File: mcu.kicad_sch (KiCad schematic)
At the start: 63 parts, among them J1 Conn_01x04_Pin, J2 USB_C_Receptacle_USB2.0_16P, J3 AudioJack2_Ground_Switch, J4 Conn_01x04_Pin, J5 Conn_01x04_Pin, J6 AudioJack2_Ground_Switch, J7 AudioJack2_Ground_Switch, Q1 BSS138, SW2 BTN, SW3 BTN, SW4 RotaryEncoder_Switch, SW5 BTN, U3 LM358B, U4 STM32G0B1RBTx

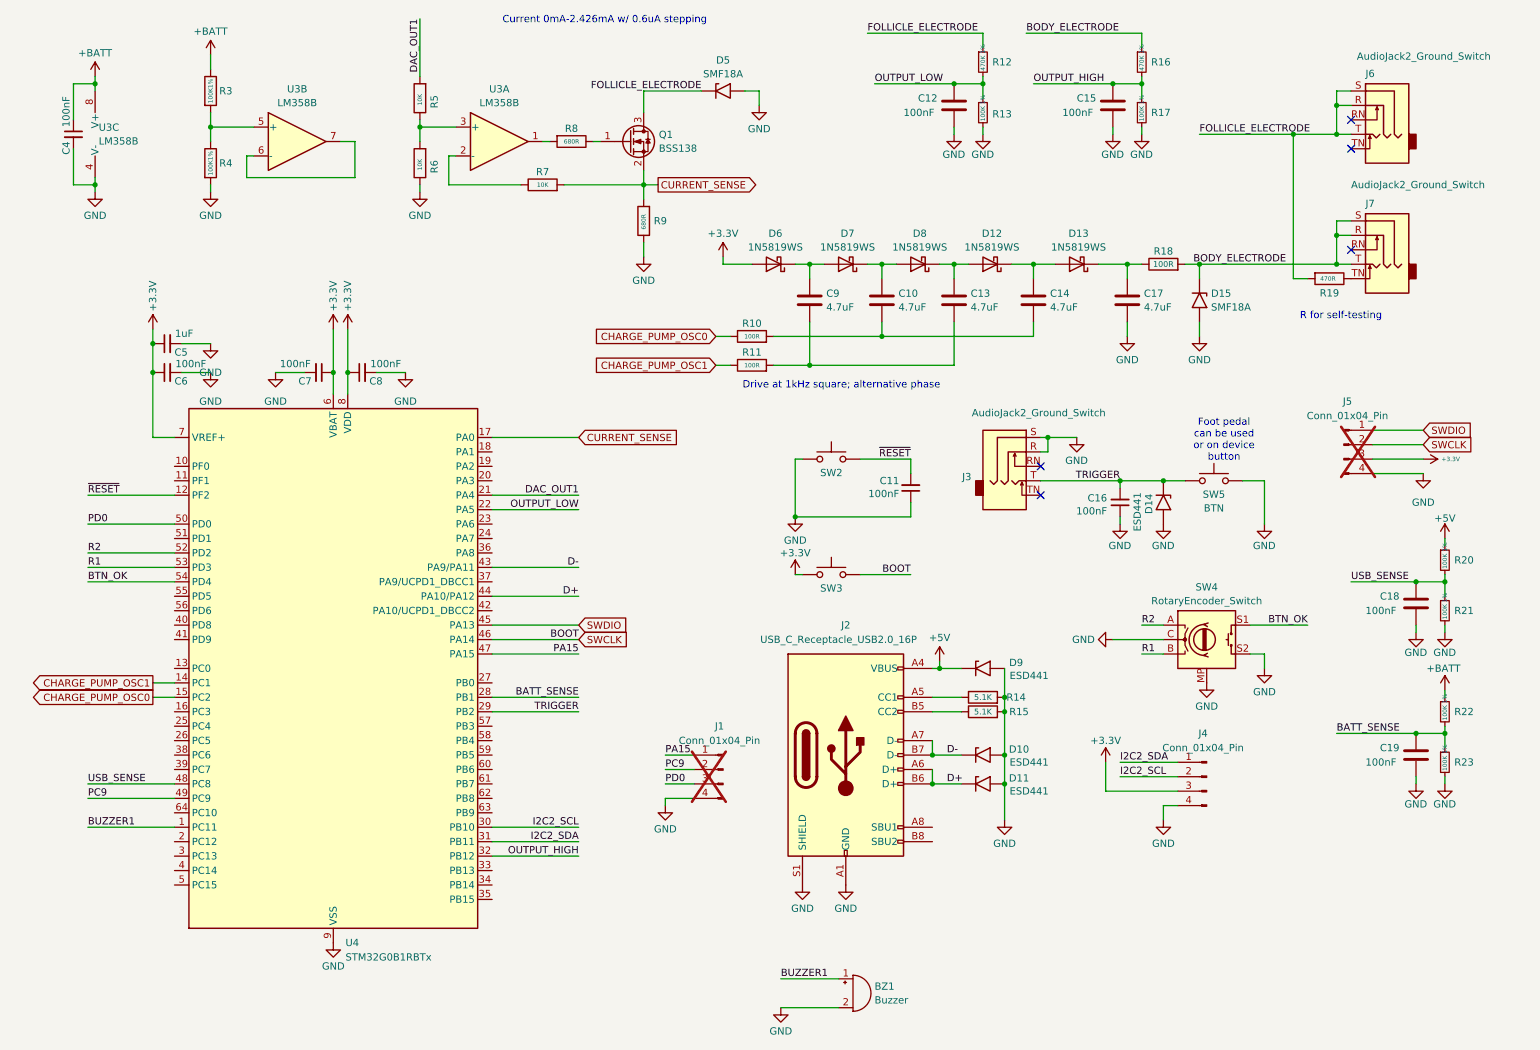
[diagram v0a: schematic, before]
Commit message: Updated buzzer and jack detection
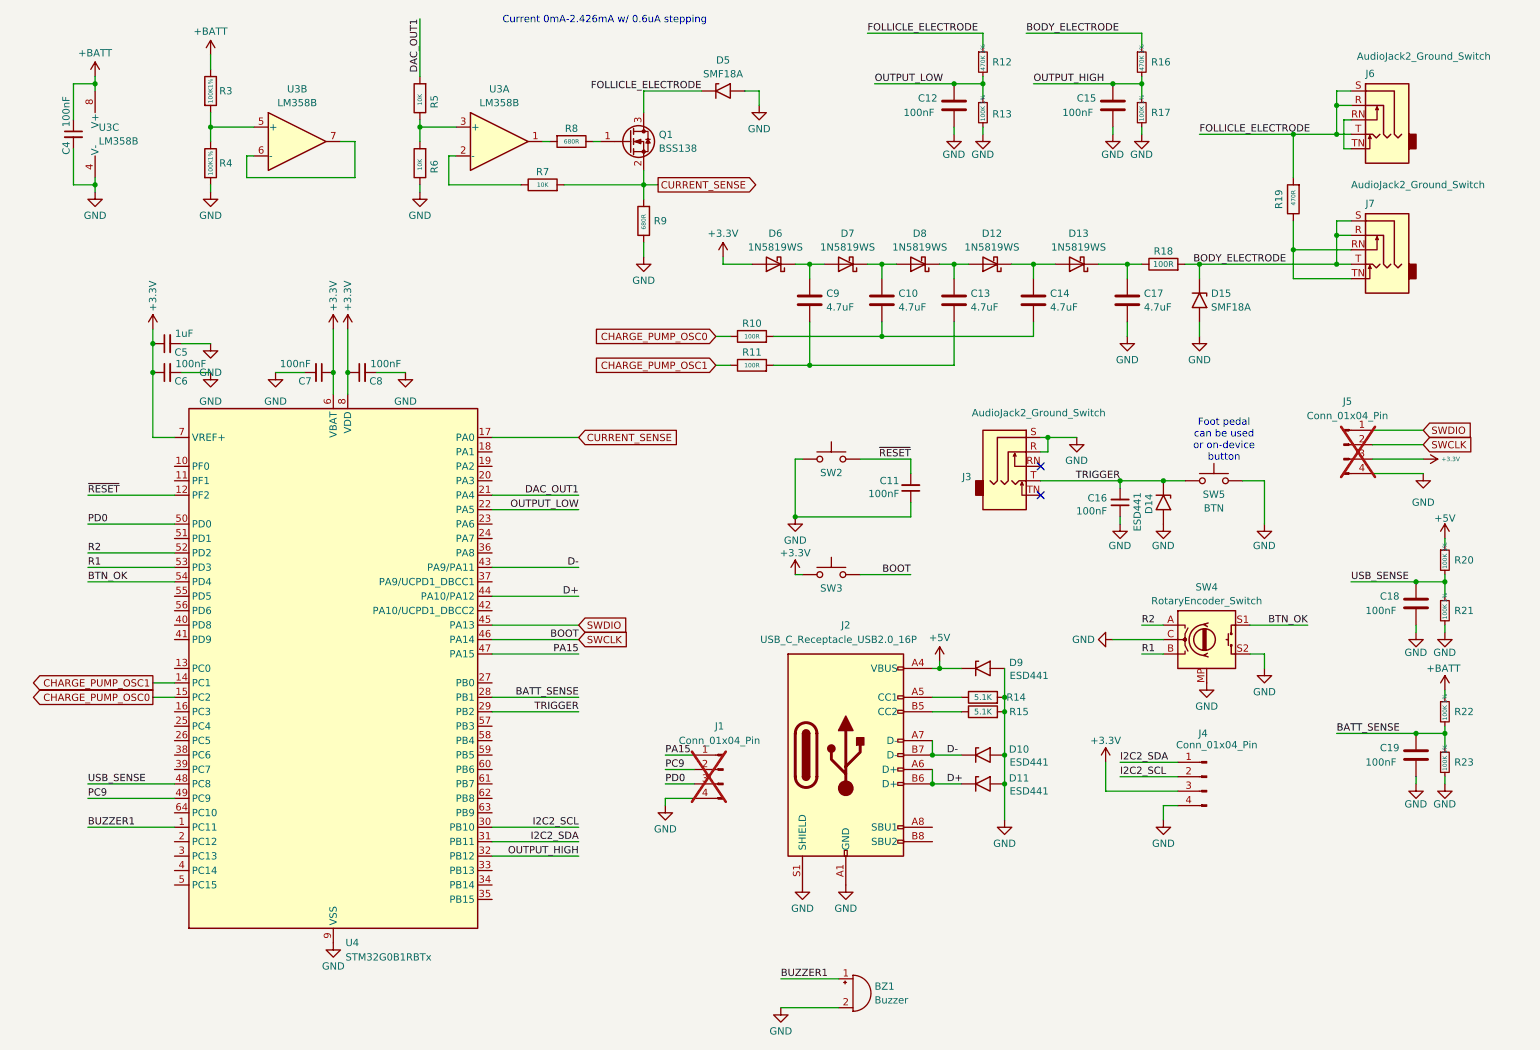
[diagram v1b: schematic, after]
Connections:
- net at J7.RN: now also J7.TN, R19.1
- net at J6.RN: now also J6.TN
- no-connect marks 5 -> 2
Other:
- note added: "Foot pedal can be used or on-device button"
- note removed: "Drive at 1kHz square; alternative phase"
- note removed: "Foot pedal can be used or on device button"
- note removed: "R for self-testing"
